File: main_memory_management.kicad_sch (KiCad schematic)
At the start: 21 parts

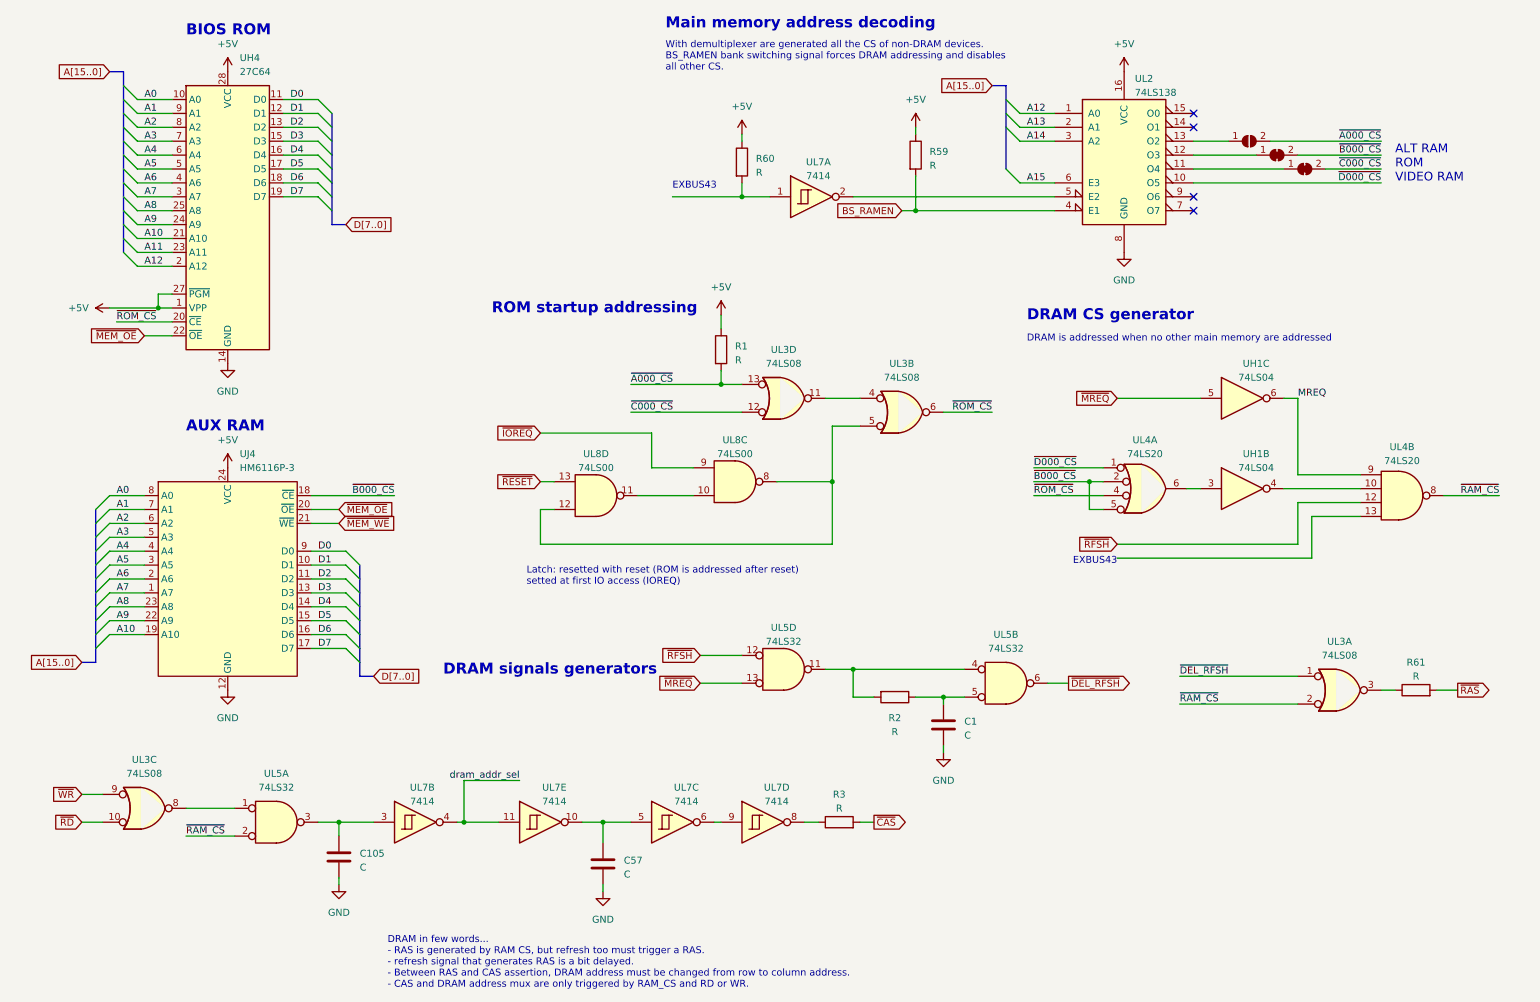
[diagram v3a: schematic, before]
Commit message: Upgrade to KiCAD 9.0
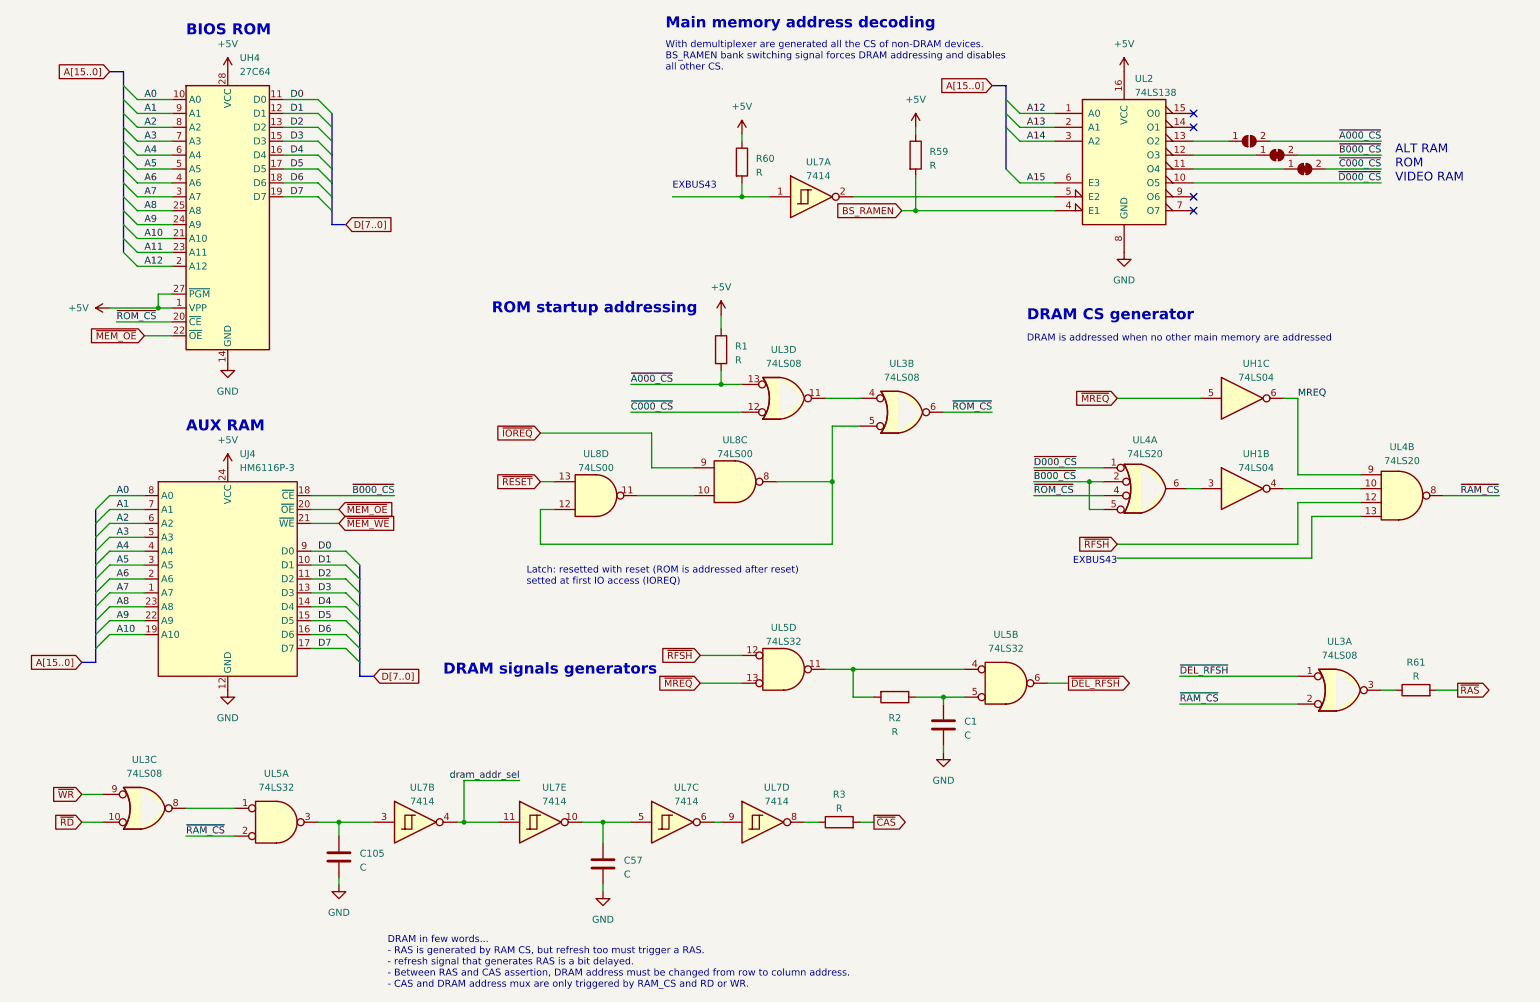
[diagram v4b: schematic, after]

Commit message: drc: updated symbols
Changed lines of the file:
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@@
 		(dnp no)
 		(fields_autoplaced yes)
-		(property "Reference" "#PWR?"
+		(property "Reference" "#PWR0225"
 			(at 33.02 68.58 0)
 			(effects
@@
 			(project "ceda"
 				(path "/12a6dbe3-008d-4c5b-88f6-9f1c816060be/4fdb1b90-7ad1-4fa0-9b13-7b81abbda2ba"
-					(reference "#PWR?")
+					(reference "#PWR0225")
 					(unit 1)
 				)
@@
 		(dnp no)
 		(fields_autoplaced yes)
-		(property "Reference" "#PWR?"
+		(property "Reference" "#PWR0239"
 			(at 176.53 39.37 0)
 			(effects
@@
 			(project "ceda"
 				(path "/12a6dbe3-008d-4c5b-88f6-9f1c816060be/4fdb1b90-7ad1-4fa0-9b13-7b81abbda2ba"
-					(reference "#PWR?")
+					(reference "#PWR0239")
 					(unit 1)
 				)
@@
 		(dnp no)
 		(fields_autoplaced yes)
-		(property "Reference" "#PWR?"
+		(property "Reference" "#PWR0235"
 			(at 140.97 73.66 0)
 			(effects
@@
 			(project "ceda"
 				(path "/12a6dbe3-008d-4c5b-88f6-9f1c816060be/4fdb1b90-7ad1-4fa0-9b13-7b81abbda2ba"
-					(reference "#PWR?")
+					(reference "#PWR0235")
 					(unit 1)
 				)
@@
 		(dnp no)
 		(fields_autoplaced yes)
-		(property "Reference" "#PWR?"
+		(property "Reference" "#PWR0236"
 			(at 214.63 29.21 0)
 			(effects
@@
 			(project "ceda"
 				(path "/12a6dbe3-008d-4c5b-88f6-9f1c816060be/4fdb1b90-7ad1-4fa0-9b13-7b81abbda2ba"
-					(reference "#PWR?")
+					(reference "#PWR0236")
 					(unit 1)
 				)
@@
 		(dnp no)
 		(fields_autoplaced yes)
-		(property "Reference" "#PWR?"
+		(property "Reference" "#PWR0240"
 			(at 144.78 40.64 0)
 			(effects
@@
 			(project "ceda"
 				(path "/12a6dbe3-008d-4c5b-88f6-9f1c816060be/4fdb1b90-7ad1-4fa0-9b13-7b81abbda2ba"
-					(reference "#PWR?")
+					(reference "#PWR0240")
 					(unit 1)
 				)
@@
 		(dnp no)
 		(fields_autoplaced yes)
-		(property "Reference" "#PWR?"
+		(property "Reference" "#PWR0228"
 			(at 50.8 101.6 0)
 			(effects
@@
 			(project "ceda"
 				(path "/12a6dbe3-008d-4c5b-88f6-9f1c816060be/4fdb1b90-7ad1-4fa0-9b13-7b81abbda2ba"
-					(reference "#PWR?")
+					(reference "#PWR0228")
 					(unit 1)
 				)
@@
 		(dnp no)
 		(fields_autoplaced yes)
-		(property "Reference" "#PWR?"
+		(property "Reference" "#PWR0224"
 			(at 50.8 29.21 0)
 			(effects
@@
 			(project "ceda"
 				(path "/12a6dbe3-008d-4c5b-88f6-9f1c816060be/4fdb1b90-7ad1-4fa0-9b13-7b81abbda2ba"
-					(reference "#PWR?")
-					(unit 1)
-				)
+					(reference "#PWR0224")
+					(unit 1)
+				)

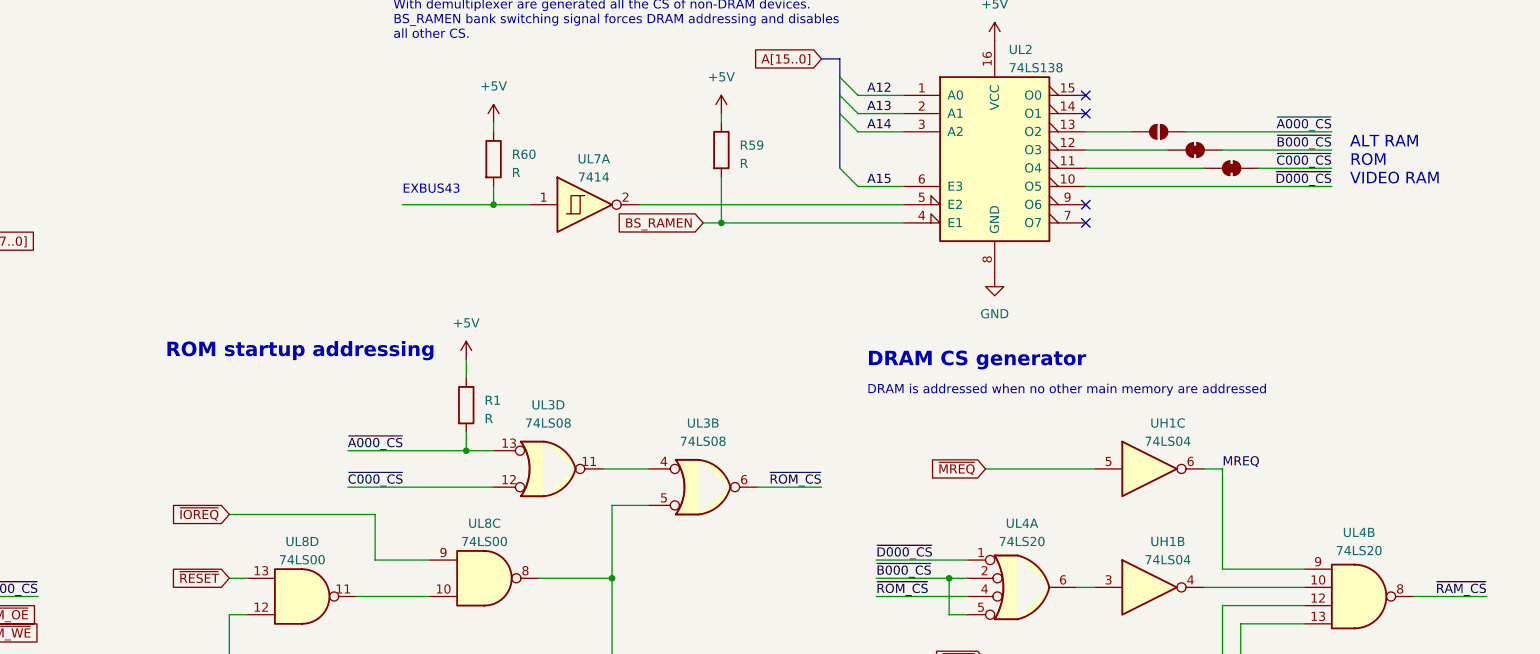
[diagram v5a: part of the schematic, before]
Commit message: drc: fixed labels
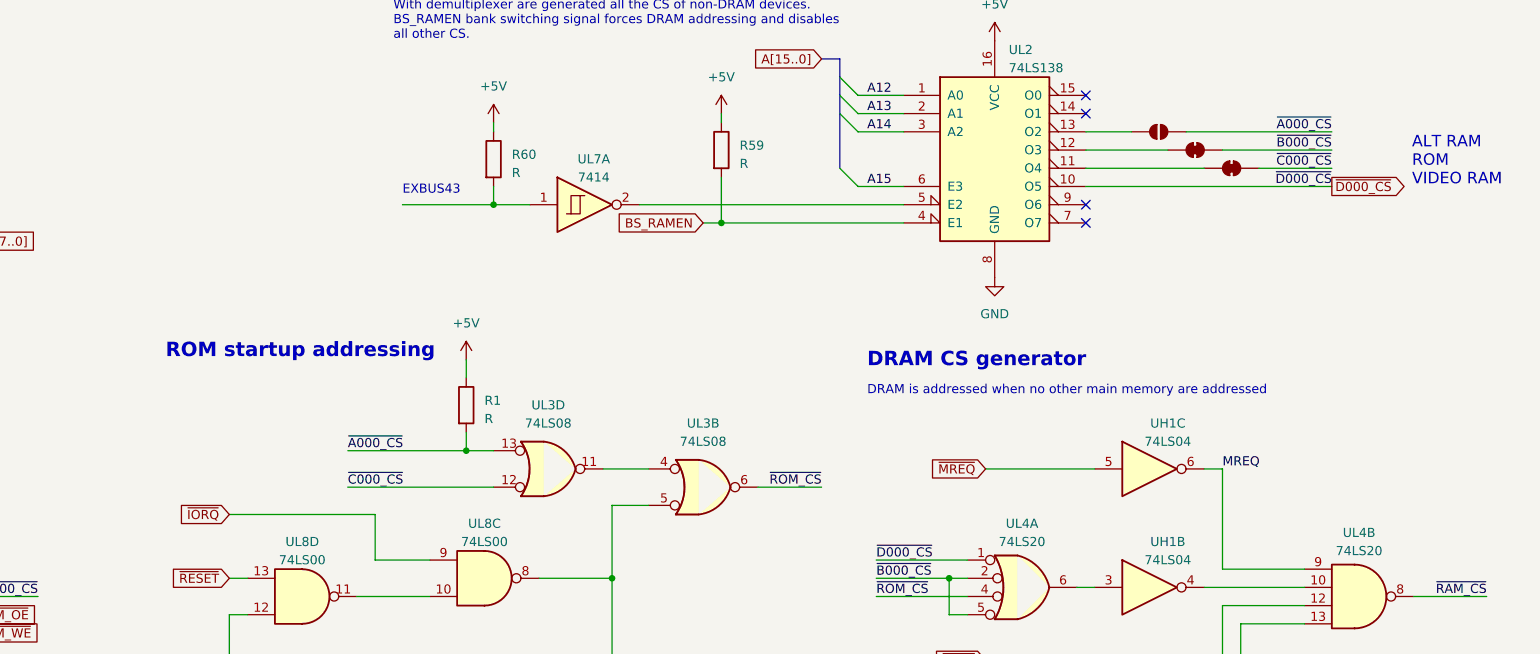
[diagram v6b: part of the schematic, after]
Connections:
- net ~{IOREQ} renamed ~{IORQ}
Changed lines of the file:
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@@
 	(text "\n\n\nALT RAM\nROM\nVIDEO RAM"
 		(exclude_from_sim no)
-		(at 264.16 45.72 0)
+		(at 272.796 45.72 0)
 		(effects
 			(font
@@
 		)
 	)
-	(global_label "~{IOREQ}"
+	(global_label "~{IORQ}"
 		(shape input)
 		(at 107.95 91.44 180)
@@
 				(hide yes)
 			)
+		)
+	)
+	(global_label "~{D000_CS}"
+		(shape output)
+		(at 261.62 45.72 0)
+		(fields_autoplaced yes)
+		(effects
+			(font
+				(size 1.27 1.27)
+			)
+			(justify left)
+		)
+		(property "Intersheetrefs" "${INTERSHEET_REFS}"
+			(at 272.9508 45.72 0)
+			(effects
+				(font
+					(size 1.27 1.27)
+				)
+				(justify left)
+				(hide yes)
+			)

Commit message: Assigned default footprints to ICs
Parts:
- UH1, UL3, UL5, UL7, UL8: footprint (none) -> Package_DIP:DIP-14_W7.62mm
- UJ4: footprint (none) -> Package_DIP:DIP-24_W7.62mm
- UL2: footprint (none) -> Package_DIP:DIP-16_W7.62mm
- UL4: footprint (none) -> Package_DIP:DIP-12_W7.62mm
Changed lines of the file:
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@@
 			)
 		)
-		(property "Footprint" ""
+		(property "Footprint" "Package_DIP:DIP-14_W7.62mm"
 			(at 152.4 85.09 0)
 			(effects
@@
 			)
 		)
-		(property "Footprint" ""
+		(property "Footprint" "Package_DIP:DIP-14_W7.62mm"
 			(at 193.04 137.16 0)
 			(effects
@@
 			)
 		)
-		(property "Footprint" ""
+		(property "Footprint" "Package_DIP:DIP-12_W7.62mm"
 			(at 265.43 102.87 0)
 			(effects
@@
 			)
 		)
-		(property "Footprint" ""
+		(property "Footprint" "Package_DIP:DIP-14_W7.62mm"
 			(at 236.22 101.6 0)
 			(effects
@@
 			)
 		)
-		(property "Footprint" ""
+		(property "Footprint" "Package_DIP:DIP-12_W7.62mm"
 			(at 218.44 101.6 0)
 			(effects
@@
 			)
 		)
-		(property "Footprint" ""
+		(property "Footprint" "Package_DIP:DIP-14_W7.62mm"
 			(at 152.4 134.62 0)
 			(effects
@@
 			)
 		)
-		(property "Footprint" ""
+		(property "Footprint" "Package_DIP:DIP-14_W7.62mm"
 			(at 143.51 100.33 0)
 			(effects
@@
 			)
 		)
-		(property "Footprint" ""
+		(property "Footprint" "Package_DIP:DIP-16_W7.62mm"
 			(at 214.63 40.64 0)
 			(effects
@@
 			)
 		)
-		(property "Footprint" ""
+		(property "Footprint" "Package_DIP:DIP-14_W7.62mm"
 			(at 35.56 160.02 0)
 			(effects
@@
 			)
 		)
-		(property "Footprint" ""
+		(property "Footprint" "Package_DIP:DIP-14_W7.62mm"
 			(at 148.59 162.56 0)
 			(effects
@@
 			)
 		)
-		(property "Footprint" ""
+		(property "Footprint" "Package_DIP:DIP-14_W7.62mm"
 			(at 236.22 85.09 0)
 			(effects
@@
 			)
 		)
-		(property "Footprint" ""
+		(property "Footprint" "Package_DIP:DIP-14_W7.62mm"
 			(at 157.48 48.26 0)
 			(effects
@@
 			)
 		)
-		(property "Footprint" ""
+		(property "Footprint" "Package_DIP:DIP-24_W7.62mm"
 			(at 50.8 100.33 0)
 			(effects
@@
 			)
 		)
-		(property "Footprint" ""
+		(property "Footprint" "Package_DIP:DIP-14_W7.62mm"
 			(at 107.95 162.56 0)
 			(effects
@@
 			)
 		)
-		(property "Footprint" ""
+		(property "Footprint" "Package_DIP:DIP-14_W7.62mm"
 			(at 132.08 162.56 0)
 			(effects
@@
 			)
 		)
-		(property "Footprint" ""
+		(property "Footprint" "Package_DIP:DIP-14_W7.62mm"
 			(at 59.69 162.56 0)
 			(effects
@@
 			)
 		)
-		(property "Footprint" ""
+		(property "Footprint" "Package_DIP:DIP-14_W7.62mm"
 			(at 118.11 102.87 0)
 			(effects
@@
 			)
 		)
-		(property "Footprint" ""
+		(property "Footprint" "Package_DIP:DIP-14_W7.62mm"
 			(at 173.99 87.63 0)
 			(effects
@@
 			)
 		)
-		(property "Footprint" ""
+		(property "Footprint" "Package_DIP:DIP-14_W7.62mm"
 			(at 85.09 162.56 0)
 			(effects
@@
 			)
 		)
-		(property "Footprint" ""
+		(property "Footprint" "Package_DIP:DIP-14_W7.62mm"
 			(at 254 138.43 0)
 			(effects

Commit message: Fixed packages
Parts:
- UJ4: footprint Package_DIP:DIP-24_W7.62mm -> Package_DIP:DIP-24_W15.24mm
- UL4: footprint Package_DIP:DIP-12_W7.62mm -> Package_DIP:DIP-14_W7.62mm
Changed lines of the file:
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@@
 			)
 		)
-		(property "Footprint" "Package_DIP:DIP-12_W7.62mm"
+		(property "Footprint" "Package_DIP:DIP-14_W7.62mm"
 			(at 265.43 102.87 0)
 			(effects
@@
 			)
 		)
-		(property "Footprint" "Package_DIP:DIP-12_W7.62mm"
+		(property "Footprint" "Package_DIP:DIP-14_W7.62mm"
 			(at 218.44 101.6 0)
 			(effects
@@
 			)
 		)
-		(property "Footprint" "Package_DIP:DIP-24_W7.62mm"
+		(property "Footprint" "Package_DIP:DIP-24_W15.24mm"
 			(at 50.8 100.33 0)
 			(effects
